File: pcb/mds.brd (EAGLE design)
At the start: 42.2 x 40 mm, 60 parts, among them IC1 MAX1555, U2 ISD1900ISD1932, U5 ATMEGA328

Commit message: Clean, code, openscad
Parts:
- R11: value ?? -> 6.8k 1%
- R12: value ?? -> 2.2k 1%
- R13: value ?? -> 10k
- R14: value ?? -> 1k5
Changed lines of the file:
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@@
 <attribute name="VALUE" x="3.175" y="6.985" size="0.6096" layer="27" rot="R90"/>
 </element>
-<element name="R11" library="rcl" package="M0805" value="??" x="12.065" y="26.035" smashed="yes">
+<element name="R11" library="rcl" package="M0805" value="6.8k 1%" x="12.065" y="26.035" smashed="yes">
 <attribute name="NAME" x="15.24" y="21.9075" size="0.8128" layer="25"/>
 <attribute name="VALUE" x="10.795" y="23.495" size="1.27" layer="27"/>
 </element>
-<element name="R12" library="rcl" package="M0805" value="??" x="12.065" y="24.13" smashed="yes" rot="R180">
+<element name="R12" library="rcl" package="M0805" value="2.2k 1%" x="12.065" y="24.13" smashed="yes" rot="R180">
 <attribute name="NAME" x="15.24" y="20.6375" size="0.8128" layer="25" rot="R180" align="top-right"/>
 <attribute name="VALUE" x="13.335" y="26.67" size="1.27" layer="27" rot="R180"/>
 </element>
-<element name="R13" library="rcl" package="M0805" value="??" x="6.35" y="23.495" smashed="yes" rot="R180">
+<element name="R13" library="rcl" package="M0805" value="10k" x="6.35" y="23.495" smashed="yes" rot="R180">
 <attribute name="NAME" x="3.81" y="24.4475" size="0.8128" layer="25" rot="R270"/>
 <attribute name="VALUE" x="7.62" y="26.035" size="1.27" layer="27" rot="R180"/>
 </element>
-<element name="R14" library="rcl" package="M0805" value="??" x="6.35" y="25.4" smashed="yes">
+<element name="R14" library="rcl" package="M0805" value="1k5" x="6.35" y="25.4" smashed="yes">
 <attribute name="NAME" x="5.3975" y="26.3525" size="0.8128" layer="25"/>
 <attribute name="VALUE" x="5.08" y="22.86" size="1.27" layer="27"/>

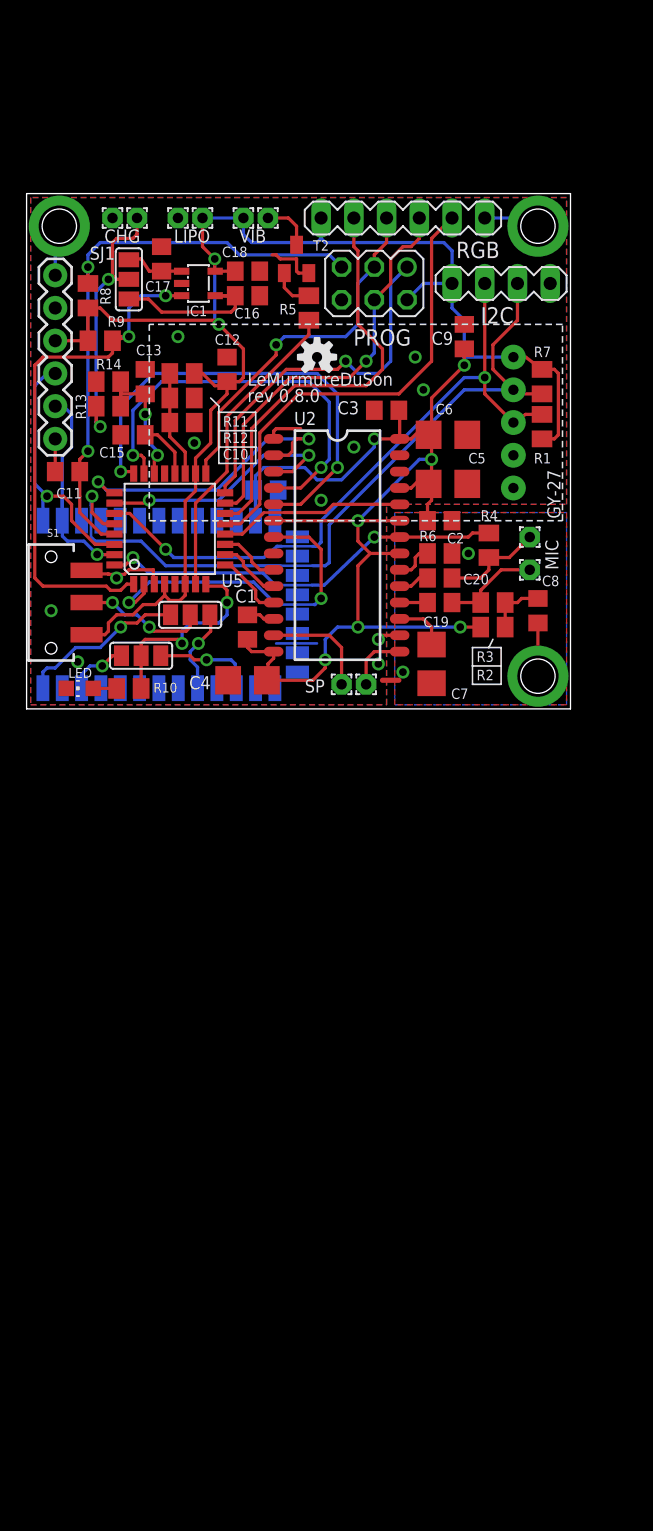
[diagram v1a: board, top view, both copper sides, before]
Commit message: Message
- MAX_BRIGHTNESS
- Welcome message
- Charged message
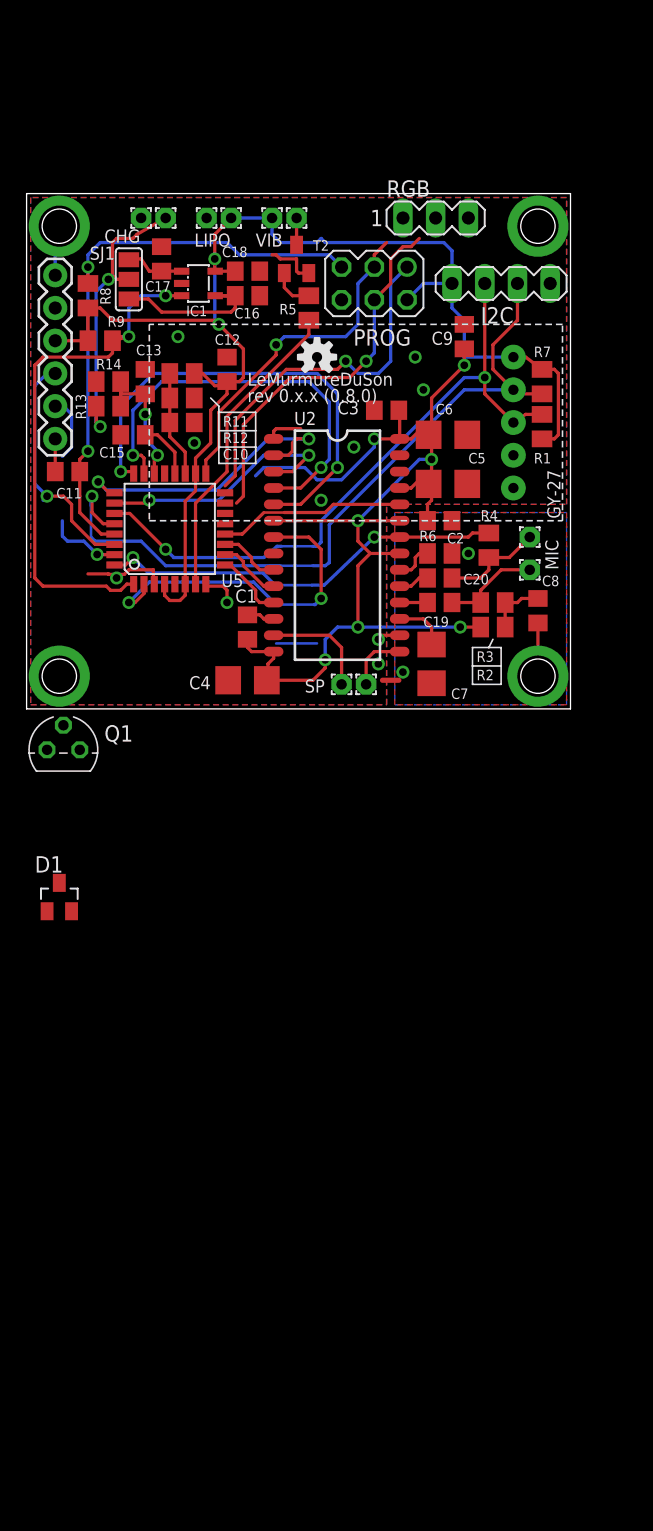
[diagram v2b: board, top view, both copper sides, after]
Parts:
- removed BLUETOOTH: HC_0x, Bluetooth HC-05:BLUETOOTH_SMD
- removed C21: 100nf, rcl:C0805
- removed LED: (no value), led:CHIP-LED0805
- removed R10: 4.7k, rcl:M0805
- removed S1: (no value), SparkFun-Electromechanical:SWITCH-SPDT-SMD
- removed SJ2, SJ3: (no value), jumper:SJ_2
- added D1: BAS40, diode:SOT23
- added Q1: BSS92, transistor-fet:TO92
- RGB: device con-lstb:MA06-1 -> con-lstb:MA03-1
- moved RGB 2.54 mm to (31.8, 38.1)
- moved LIPO+ 2.22 mm to (15.9, 38.1)
- moved LIPO- 2.22 mm to (14.0, 38.1)
- moved PWR+ 2.22 mm to (10.8, 38.1)
- moved PWR- 2.22 mm to (8.89, 38.1)
- moved VIB+ 2.22 mm to (19.1, 38.1)
- moved VIB- 2.22 mm to (21.0, 38.1)
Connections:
- removed net HC05_KEY: BLUETOOTH.34, SJ2.3
- removed net HC05_LED: BLUETOOTH.32, SJ3.3
- removed net HC06_KEY: BLUETOOTH.26, SJ2.1
- removed net HC06_LED: BLUETOOTH.24, SJ3.1
- removed net N$10: LED.A, R10.1
- removed net SI: RGB.5, U5.13
- removed net SS: RGB.2, U5.14
- new net PWR_CMD: D1.1, Q1.1, U5.13
- net CHG: now also D1.3
- net GND: now also RGB.3; no longer BLUETOOTH.13, BLUETOOTH.21, BLUETOOTH.22, C21.1, LED.C, RGB.6, S1.3
- net LEDB: no longer R10.2, SJ3.2
- net MISO: no longer U5.16
- net MOSI: no longer RGB.4, U5.15
- net N$4: now also Q1.3; no longer S1.2, SJ2.2
- net RXI: no longer BLUETOOTH.1
- net SCK: now also RGB.2; no longer RGB.3
- net TXO: no longer BLUETOOTH.2
- net VCC: now also Q1.2; no longer BLUETOOTH.12, C21.2, S1.1
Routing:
- net SI: track 36.3 -> 0.00 mm
- net SS: track 32.8 -> 0.00 mm
- net VCC: track 212.1 -> 194.7 mm
- net HC05_KEY: track 13.0 -> 0.00 mm, vias 1 -> 0
- net LEDB: track 15.7 -> 2.83 mm, vias 2 -> 1
- net N$4: track 10.0 -> 0.00 mm, vias 2 -> 0
- net HC06_LED: track 7.94 -> 0.00 mm, vias 1 -> 0
- net TXO: track 17.7 -> 10.9 mm
- net HC06_KEY: track 6.60 -> 0.00 mm, vias 1 -> 0
- net HC05_LED: track 4.77 -> 0.00 mm, vias 1 -> 0
- net GND: track 34.2 -> 29.5 mm, vias 16 -> 15
- net MOSI: track 32.0 -> 29.5 mm
- net SCK: track 28.4 -> 26.5 mm
- net N$7: track 3.93 -> 2.08 mm
- net N$10: track 1.81 -> 0.00 mm
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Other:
- board text added: "rev 0.x.x (0.8.0)"
- board text removed: "rev 0.8.0"

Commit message: Power control
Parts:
- removed D1: BAS40, diode:SOT23
- removed Q1: BSS92, transistor-fet:TO92
- added D3, D4: (no value), OPL Eagle Library:LL-34
- added LDR+, LDR-: (no value), wirepad:1,6/0,8
- added Q2: MOSFET-P, OPL Eagle Library:SOT23
- added R10, R15: 4.7k, rcl:M0805
- added U$1: HMC5883LSMD, SparkFun-Sensors:16LPCC
- added U3: ADXL345, SparkFun-Sensors:LGA14
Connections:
- removed net N$4: Q1.3
- new net +UB: LIPO+.1, Q2.2
- new net AD_INT1: U3.8, U5.14
- new net AD_INT2: U3.9, U5.15
- new net LDR: LDR-.1, R15.2
- new net N$13: U5.16
- new net N$14: U$1.8
- new net N$9: D4.C
- net CHG: now also D3.C; no longer D1.3
- net GND: now also R15.1, U$1.11, U$1.9, U3.11, U3.2, U3.3, U3.4, U3.5
- net PWR_CMD: now also D3.A, D4.A, Q2.1, R10.1; no longer D1.1, Q1.1
- net SCL: now also U3.14
- net SDA: now also U3.13
- net VCC: now also LDR+.1, Q2.3, R10.2, U$1.13, U$1.2, U$1.4, U3.1, U3.6; no longer LIPO+.1, Q1.2
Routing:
- net VCC: track 194.7 -> 189.8 mm
- net AD1: track 10.5 -> 8.59 mm
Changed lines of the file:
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@@
 <layer number="113" name="Dim" color="13" fill="1" visible="no" active="yes"/>
 <layer number="116" name="Patch_BOT" color="9" fill="4" visible="no" active="yes"/>
+<layer number="118" name="Rect_Pads" color="7" fill="1" visible="no" active="no"/>
 <layer number="121" name="_tsilk" color="7" fill="1" visible="no" active="yes"/>
 <layer number="122" name="_bsilk" color="7" fill="1" visible="no" active="yes"/>
@@
 <attribute name="OC_FARNELL" value="unknown" x="31.75" y="38.1" size="1.778" layer="27" display="off"/>
 </element>
-<element name="Q1" library="transistor-fet" package="TO92" value="BSS92" x="2.8575" y="-3.175"/>
-<element name="D1" library="diode" package="SOT23" value="BAS40" x="2.54" y="-14.605"/>
+<element name="R10" library="rcl" package="M0805" value="4.7k" x="2.2225" y="-28.575"/>
+<element name="Q2" library="OPL Eagle Library" package="SOT23" value="MOSFET-P" x="2.54" y="-34.925"/>
+<element name="D3" library="OPL Eagle Library" package="LL-34" value="" x="2.54" y="-39.37"/>
+<element name="D4" library="OPL Eagle Library" package="LL-34" value="" x="2.54" y="-43.18"/>
+<element name="U3" library="SparkFun-Sensors" package="LGA14" value="ADXL345" x="9.8425" y="4.445"/>
+<element name="U$1" library="SparkFun-Sensors" package="16LPCC" value="HMC5883LSMD" x="14.9225" y="6.0325"/>
+<element name="R15" library="rcl" package="M0805" value="4.7k" x="2.2225" y="-47.3075"/>
+<element name="LDR-" library="wirepad" package="1,6/0,8" value="" x="1.27" y="-57.15"/>
+<element name="LDR+" library="wirepad" package="1,6/0,8" value="" x="1.27" y="-60.96"/>
 </elements>
 <signals>
@@
 <via x="2.54" y="2.54" extent="1-16" drill="3.2" diameter="4.7498"/>
 <via x="39.6875" y="37.465" extent="1-16" drill="3.2" diameter="4.7498"/>
+<contactref element="U3" pad="3"/>
+<contactref element="U3" pad="2"/>
+<contactref element="U3" pad="11"/>
+<contactref element="U3" pad="5"/>
+<contactref element="U3" pad="4"/>
+<contactref element="U$1" pad="9"/>
+<contactref element="U$1" pad="11"/>
+<contactref element="R15" pad="1"/>
 <wire x1="40.64" y1="33.02" x2="39.6875" y2="37.465" width="0" layer="19" extent="1-1"/>
-<wire x1="2.54" y1="2.54" x2="4.7625" y2="10.4775" width="0" layer="19" extent="1-1"/>
+<wire x1="16.2925" y1="6.2825" x2="17.145" y2="7.3" width="0" layer="19" extent="1-1"/>
+<wire x1="16.2925" y1="5.2825" x2="16.2925" y2="6.2825" width="0" layer="19" extent="1-1"/>
+<wire x1="2.54" y1="2.54" x2="8.6425" y2="5.545" width="0" layer="19" extent="1-1"/>
+<wire x1="1.2725" y1="-47.3075" x2="2.54" y2="2.54" width="0" layer="19" extent="1-1"/>
 </signal>
 <signal name="MIC+">
@@
 <wire x1="25.7175" y1="11.1125" x2="26.67" y2="12.065" width="0.254" layer="1"/>
 <contactref element="R9" pad="2"/>
-<contactref element="LIPO+" pad="1"/>
 <contactref element="VIB+" pad="1"/>
 <wire x1="19.05" y1="36.83" x2="19.05" y2="38.1" width="0.254" layer="16"/>
 <wire x1="14.605" y1="34.925" x2="14.605" y2="36.83" width="0.254" layer="1"/>
-<wire x1="14.605" y1="36.83" x2="15.875" y2="38.1" width="0.254" layer="1"/>
-<wire x1="15.875" y1="38.1" x2="19.05" y2="38.1" width="0.254" layer="16"/>
 <wire x1="14.9225" y1="29.845" x2="14.605" y2="30.1625" width="0.254" layer="1"/>
 <wire x1="14.605" y1="30.1625" x2="6.6675" y2="30.1625" width="0.254" layer="1"/>
@@
 <wire x1="10.7125" y1="8.81375" x2="10.7125" y2="8.8075" width="0.254" layer="1"/>
 <contactref element="RGB" pad="1"/>
-<contactref element="Q1" pad="2"/>
+<contactref element="R10" pad="2"/>
+<contactref element="Q2" pad="3"/>
+<contactref element="U3" pad="1"/>
+<contactref element="U3" pad="6"/>
+<contactref element="U$1" pad="13"/>
+<contactref element="U$1" pad="2"/>
+<contactref element="U$1" pad="4"/>
+<contactref element="LDR+" pad="1"/>
 <wire x1="32.385" y1="36.195" x2="29.21" y2="38.1" width="0" layer="19" extent="16-16"/>
-<wire x1="2.8575" y1="-1.27" x2="11.1125" y2="8.41375" width="0" layer="19" extent="1-1"/>
+<wire x1="15.6725" y1="7.4025" x2="17.145" y2="5.4" width="0" layer="19" extent="1-1"/>
+<wire x1="13.5525" y1="6.2825" x2="15.6725" y2="7.4025" width="0" layer="19" extent="1-1"/>
+<wire x1="13.5525" y1="5.2825" x2="13.5525" y2="6.2825" width="0" layer="19" extent="1-1"/>
+<wire x1="11.8425" y1="5.545" x2="13.5525" y2="5.2825" width="0" layer="19" extent="1-1"/>
+<wire x1="11.90625" y1="8.41375" x2="13.5525" y2="6.2825" width="0" layer="19" extent="1-1"/>
+<wire x1="7.8425" y1="5.545" x2="11.8425" y2="5.545" width="0" layer="19" extent="1-1"/>
+<wire x1="3.1725" y1="-28.575" x2="7.8425" y2="5.545" width="0" layer="19" extent="1-1"/>
+<wire x1="2.54" y1="-33.909" x2="3.1725" y2="-28.575" width="0" layer="19" extent="1-1"/>
+<wire x1="1.27" y1="-60.96" x2="2.54" y2="-33.909" width="0" layer="19" extent="1-1"/>
 </signal>
 <signal name="N$5">
@@
 <wire x1="8.0075" y1="15.17" x2="10.795" y2="12.3825" width="0.254" layer="1"/>
 <via x="10.795" y="12.3825" extent="1-16" drill="0.6"/>
+<contactref element="U3" pad="13"/>
+<wire x1="11.8425" y1="3.345" x2="11.43" y2="11.7475" width="0" layer="19" extent="1-16"/>
 </signal>
 <signal name="SCL">
@@
 <wire x1="6.8199" y1="14.37" x2="5.95" y2="14.37" width="0.254" layer="1"/>
 <wire x1="5.95" y1="14.37" x2="5.08" y2="15.24" width="0.254" layer="1"/>
+<contactref element="U3" pad="14"/>
+<wire x1="11.9425" y1="4.445" x2="10.795" y2="11.1125" width="0" layer="19" extent="1-16"/>
 </signal>
 <signal name="AREF">
@@
 <wire x1="7.77875" y1="9.68375" x2="7.29615" y2="9.20115" width="0.254" layer="1"/>
 <wire x1="7.29615" y1="9.20115" x2="6.5151" y2="9.20115" width="0.254" layer="1"/>
-<contactref element="D1" pad="3"/>
-<wire x1="6.5151" y1="9.20115" x2="2.54" y2="-13.505" width="0" layer="19" extent="1-1"/>
+<contactref element="D3" pad="C"/>
+<wire x1="6.5151" y1="9.20115" x2="4.064" y2="-39.37" width="0" layer="19" extent="1-1"/>
 </signal>
 <signal name="MISO">
@@
 </signal>
 <signal name="AD1">
-<contactref element="C13" pad="1"/>
-<contactref element="U5" pad="22"/>
 <contactref element="R13" pad="1"/>
 <contactref element="R14" pad="2"/>
 <wire x1="7.3" y1="25.4" x2="7.3" y2="24.4475" width="0.254" layer="1"/>
 <wire x1="7.3" y1="24.4475" x2="7.3" y2="23.495" width="0.254" layer="1"/>
+<wire x1="7.3025" y1="24.45" x2="7.3" y2="24.4475" width="0.254" layer="1"/>
+<contactref element="C13" pad="1"/>
+<contactref element="U5" pad="22"/>
 <wire x1="9.9125" y1="18.2626" x2="9.9125" y2="19.4375" width="0.254" layer="1"/>
 <wire x1="9.9125" y1="19.4375" x2="10.16" y2="19.685" width="0.254" layer="1"/>
@@
 <via x="9.2075" y="22.86" extent="1-16" drill="0.6"/>
 <wire x1="9.2075" y1="22.86" x2="9.2075" y2="24.45" width="0.254" layer="1"/>
-<wire x1="9.2075" y1="24.45" x2="7.3025" y2="24.45" width="0.254" layer="1"/>
-<wire x1="7.3025" y1="24.45" x2="7.3" y2="24.4475" width="0.254" layer="1"/>
+<wire x1="9.2075" y1="24.45" x2="7.3" y2="24.4475" width="0" layer="19" extent="1-1"/>
 </signal>
 <signal name="LEDB">
@@
 <signal name="PWR_CMD">
 <contactref element="U5" pad="13"/>
-<contactref element="Q1" pad="1"/>
-<contactref element="D1" pad="1"/>
-<wire x1="4.1275" y1="-3.175" x2="15.4051" y2="14.37" width="0" layer="19" extent="1-1"/>
-<wire x1="1.59" y1="-15.705" x2="4.1275" y2="-3.175" width="0" layer="19" extent="1-1"/>
-</signal>
-<signal name="N$4">
-<contactref element="Q1" pad="3"/>
+<contactref element="R10" pad="1"/>
+<contactref element="Q2" pad="1"/>
+<contactref element="D4" pad="A"/>
+<contactref element="D3" pad="A"/>
+<wire x1="1.016" y1="-39.37" x2="1.016" y2="-43.18" width="0" layer="19" extent="1-1"/>
+<wire x1="1.651" y1="-35.941" x2="1.016" y2="-39.37" width="0" layer="19" extent="1-1"/>
+<wire x1="1.2725" y1="-28.575" x2="1.651" y2="-35.941" width="0" layer="19" extent="1-1"/>
+<wire x1="15.4051" y1="14.37" x2="1.2725" y2="-28.575" width="0" layer="19" extent="1-1"/>
+</signal>
+<signal name="+UB">
+<contactref element="Q2" pad="2"/>
+<contactref element="LIPO+" pad="1"/>
+<wire x1="3.429" y1="-35.941" x2="15.875" y2="38.1" width="0" layer="19" extent="1-1"/>
+</signal>
+<signal name="N$9">
+<contactref element="D4" pad="C"/>
+</signal>
+<signal name="AD_INT1">
+<contactref element="U3" pad="8"/>
+<contactref element="U5" pad="14"/>
+<wire x1="7.8425" y1="3.345" x2="15.4051" y2="15.17" width="0" layer="19" extent="1-1"/>
+</signal>
+<signal name="AD_INT2">
+<contactref element="U3" pad="9"/>
+<contactref element="U5" pad="15"/>
+<wire x1="8.6425" y1="3.345" x2="15.4051" y2="15.97" width="0" layer="19" extent="1-1"/>
+</signal>
+<signal name="N$14">
+<contactref element="U$1" pad="8"/>
+</signal>
+<signal name="N$13">
+<contactref element="U5" pad="16"/>
+</signal>
+<signal name="LDR">
+<contactref element="LDR-" pad="1"/>
+<contactref element="R15" pad="2"/>
+<wire x1="3.1725" y1="-47.3075" x2="1.27" y2="-57.15" width="0" layer="19" extent="1-1"/>
 </signal>
 </signals>
